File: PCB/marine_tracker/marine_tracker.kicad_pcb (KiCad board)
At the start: 2 copper layers, 71.7 x 36.4 mm, 38 parts, among them J1 Screw_Terminal_01x02, J2 Conn_ARM_JTAG_SWD_10, J4 BM04B-GHS-TBT, J5 molex_533981071, SW1 SW_Push, U1 STM32U575RGT6, U2 SHT40, U4 MIC5504-3.3YM5, U5 SAM-M10Q, U6 25CSM04T-I/SN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

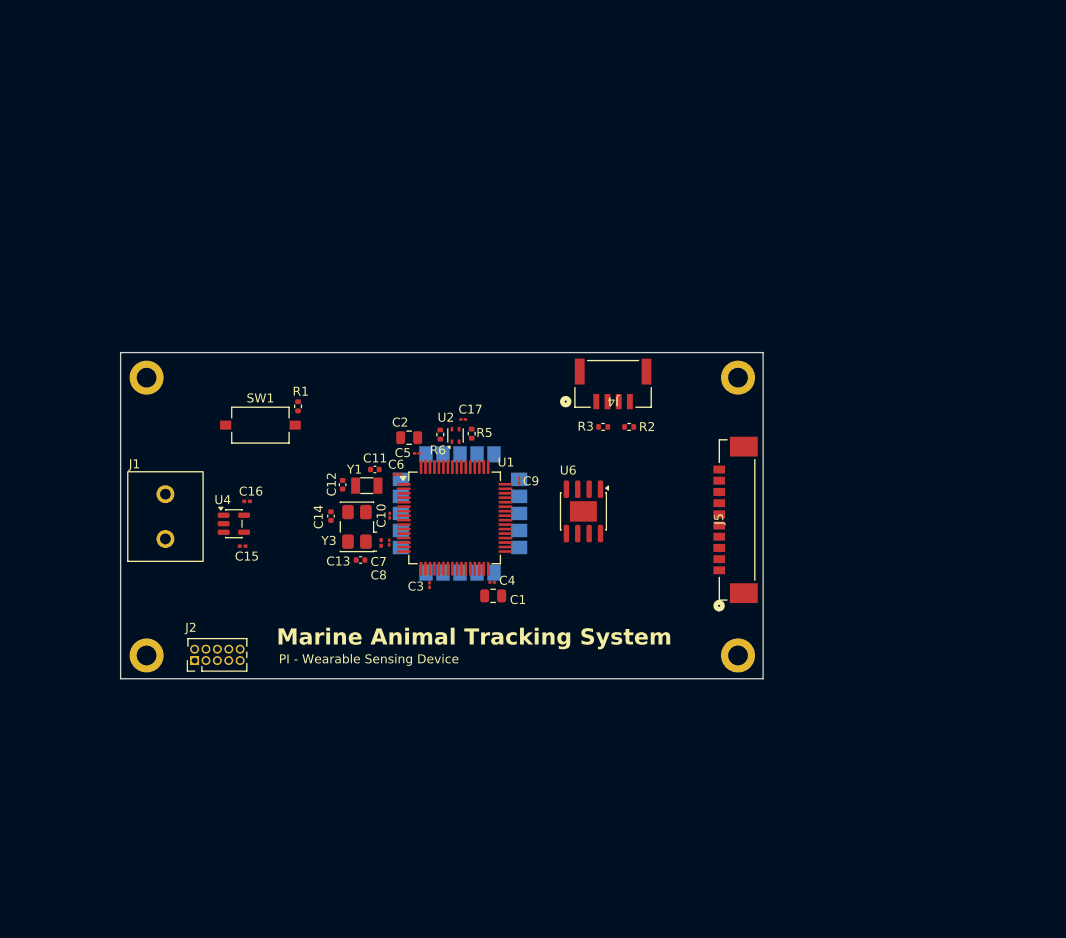
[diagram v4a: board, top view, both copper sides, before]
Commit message: routage + change GNSS module + add decoupling capacitor + change 0200/0400 package to 0600 package
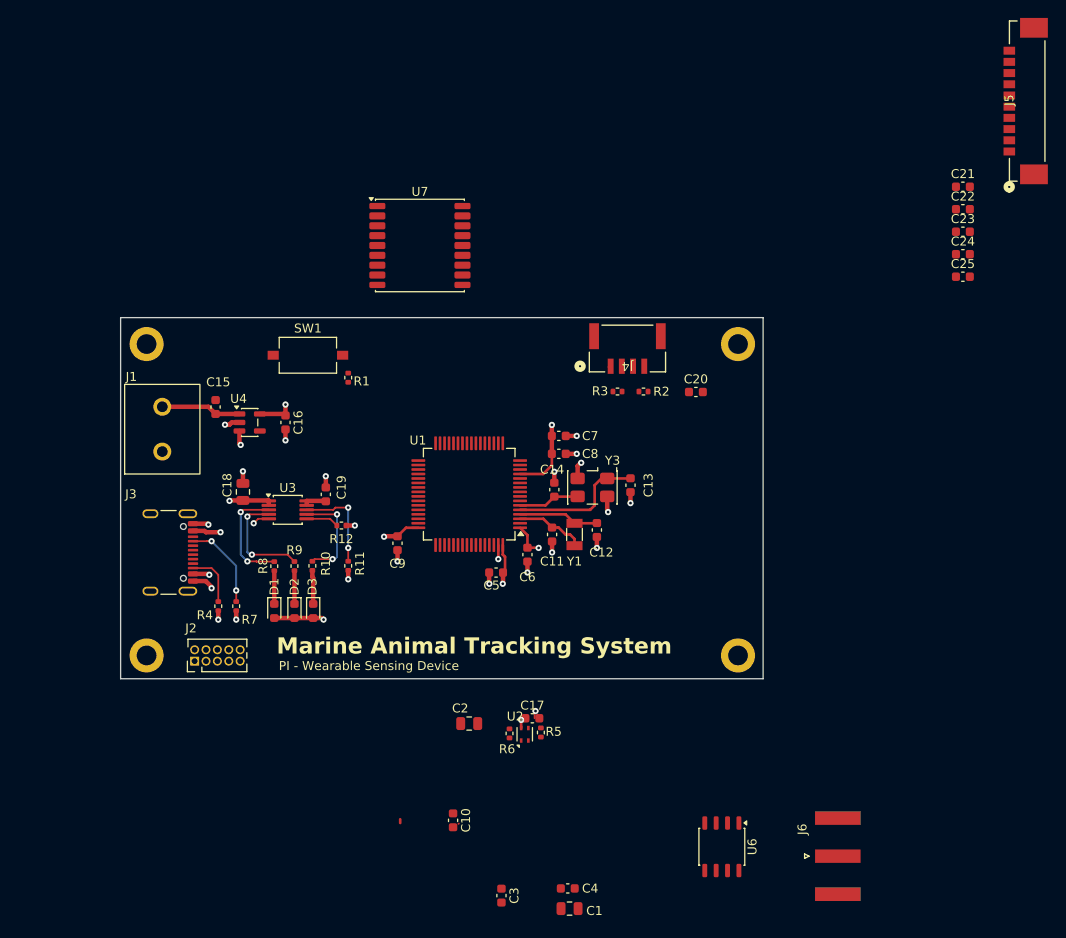
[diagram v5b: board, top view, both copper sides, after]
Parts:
- removed U5: SAM-M10Q, Beuns_PCBFootprint:XCVR_SAM-M10Q-00B
- added C18: 10u, Capacitor_SMD:C_0805_2012Metric, F.Cu at (52.2, 83.8)
- added C19: 1u, Capacitor_SMD:C_0603_1608Metric, F.Cu at (61.5, 84.0)
- added C20: 100n, Capacitor_SMD:C_0603_1608Metric, F.Cu at (102.8, 72.6)
- added C21: 100n, Capacitor_SMD:C_0603_1608Metric, F.Cu at (132.6, 49.7)
- added C22: 1n, Capacitor_SMD:C_0603_1608Metric, F.Cu at (132.6, 52.2)
- added C23: 100n, Capacitor_SMD:C_0603_1608Metric, F.Cu at (132.6, 54.7)
- added C24: 1n, Capacitor_SMD:C_0603_1608Metric, F.Cu at (132.6, 57.2)
- added C25: 100n, Capacitor_SMD:C_0603_1608Metric, F.Cu at (132.6, 59.7)
- added D1: LED, LED_SMD:LED_0603_1608Metric, F.Cu at (55.8, 97.0)
- added D2: LED, LED_SMD:LED_0603_1608Metric, F.Cu at (58.0, 97.0)
- added D3: LED, LED_SMD:LED_0603_1608Metric, F.Cu at (60.1, 97.0)
- added J3: USB_C_Receptacle_USB2.0_16P, Connector_USB:USB_C_Receptacle_GCT_USB4105-xx-A_16P_TopMnt_Horizontal, F.Cu at (43.0, 90.5)
- added J6: Conn_Coaxial, Connector_Coaxial:SMA_Amphenol_132289_EdgeMount, F.Cu at (118.6, 124.4)
- added R10: 470, Resistor_SMD:R_0402_1005Metric, F.Cu at (60.0, 92.0)
- added R11: 10k, Resistor_SMD:R_0402_1005Metric, F.Cu at (64.0, 92.0)
- added R12: 1k, Resistor_SMD:R_0402_1005Metric, F.Cu at (63.2, 87.5)
- added R4: 5k1, Resistor_SMD:R_0402_1005Metric, F.Cu at (49.5, 96.5)
- added R7: 5k1, Resistor_SMD:R_0402_1005Metric, F.Cu at (51.5, 96.5)
- added R8: 470, Resistor_SMD:R_0402_1005Metric, F.Cu at (55.8, 92.0)
- added R9: 470, Resistor_SMD:R_0402_1005Metric, F.Cu at (58.0, 92.0)
- added U3: MCP73833-xxx-UN, Package_SO:MSOP-10_3x3mm_P0.5mm, F.Cu at (57.2, 85.8)
- added U7: MAX-M10S, RF_GPS:ublox_MAX, F.Cu at (72.0, 56.2)
- C10, C17, C3, C4, C5, C8, C9: footprint Capacitor_SMD:C_01005_0402Metric -> Capacitor_SMD:C_0603_1608Metric
- C11, C12, C13, C14: footprint Capacitor_SMD:C_0402_1005Metric -> Capacitor_SMD:C_0603_1608Metric
- C15, C16, C6, C7: footprint Capacitor_SMD:C_0201_0603Metric -> Capacitor_SMD:C_0603_1608Metric
- U6: footprint Package_SO:SOIC-8-1EP_3.9x4.9mm_P1.27mm_EP2.29x3mm -> Package_SO:JEITA_SOIC-8_3.9x4.9mm_P1.27mm
- moved J5 56.9 mm to (139.8, 40.1)
- moved U6 40.5 mm to (105.7, 123.3)
- moved C1 35.9 mm to (88.7, 130.2)
- moved C3 35.6 mm to (81.1, 128.8)
- moved C4 35.2 mm to (88.5, 128.0)
- moved C10 34.7 mm to (75.7, 120.4)
- moved C17 34.2 mm to (84.5, 109.0)
- moved R6 34.2 mm to (82.0, 110.7)
- moved R5 34.2 mm to (85.5, 110.6)
- moved U2 34.2 mm to (83.7, 110.8)
- moved C2 32.6 mm to (77.5, 109.6)
- moved C13 31.3 mm to (95.5, 83.0), turned to 90 degrees
- moved C12 28.8 mm to (91.8, 88.0), turned to 90 degrees
- moved Y3 26.6 mm to (91.2, 83.2), turned to 180 degrees
- moved C14 25.1 mm to (87.0, 83.5), turned to -90 degrees
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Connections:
- net MEM_SPI1_CS renamed MEM_SPI3_CS
- U1 pad 15: MEM_SPI1_SCK -> unconnected-(U1-PA1-Pad15)
- U1 pad 44: MEM_SPI1_MISO -> USB_D-
- U1 pad 45: MEM_SPI1_MOSI -> USB_D+
- U1 pad 51: unconnected-(U1-PC10-Pad51) -> MEM_SPI1_SCK
- U1 pad 52: unconnected-(U1-PC11-Pad52) -> MEM_SPI3_MISO
- U1 pad 53: unconnected-(U1-PC12-Pad53) -> MEM_SPI3_MOSI
- U1 pad 56: unconnected-(U1-PB4-Pad56) -> GPS_LNA_EN
- U6 pad 2: MEM_SPI1_MISO -> MEM_SPI3_MISO
- U6 pad 5: MEM_SPI1_MOSI -> MEM_SPI3_MOSI
- U6 pad 6: MEM_SPI1_SCK -> MEM_SPI3_SCK
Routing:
- net GND: track 0.00 -> 34.3 mm, vias 0 -> 25
- net +3V3: track 0.00 -> 25.7 mm, vias 0 -> 5
- net VBUS: track 0.00 -> 15.4 mm, vias 0 -> 4
- net /HSE_IN: track 0.00 -> 15.1 mm
- net +BATT: track 0.00 -> 13.1 mm, vias 0 -> 1
- net /STAT1: track 0.00 -> 12.3 mm, vias 0 -> 2
- net /STAT2: track 0.00 -> 12.2 mm, vias 0 -> 2
- net /PG: track 0.00 -> 11.1 mm, vias 0 -> 2
- net /THERM: track 0.00 -> 10.7 mm, vias 0 -> 2
- net /USB_CC1: track 0.00 -> 9.95 mm, vias 0 -> 2
- net /LSE_OUT: track 0.00 -> 9.00 mm
- net /LSE_IN: track 0.00 -> 8.03 mm
- net /HSE_OUT: track 0.00 -> 6.84 mm
- net /USB_CC2: track 0.00 -> 6.12 mm
- net /LED3: track 0.00 -> 3.74 mm
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- added copper zone on In2.Cu, net +3V3
- added copper zone on In2.Cu, net +BATT
- added copper zone on In1.Cu, net GND
- added copper zone on In2.Cu, net VBUS
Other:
- board size 71.7 x 36.4 mm -> 71.7 x 40.3 mm
- copper layers 2 -> 4

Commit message: PCB routage WIP
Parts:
- moved C25 72.1 mm to (71.0, 97.2), turned to 180 degrees
- moved C1 56.7 mm to (74.0, 75.5), turned to 90 degrees
- moved C4 52.4 mm to (78.8, 76.5), turned to 90 degrees
- moved C3 52.3 mm to (71.0, 77.5), turned to 180 degrees
- moved U7 45.1 mm to (109.0, 82.0)
- moved U6 43.0 mm to (69.0, 101.0), turned to 0 degrees
- moved C20 41.9 mm to (60.9, 72.2), turned to 180 degrees
- moved J6 39.6 mm to (122.6, 85.0)
- moved C2 35.2 mm to (70.8, 75.0)
- moved R2 31.9 mm to (65.1, 72.5)
- moved J4 31.4 mm to (63.8, 67.7)
- moved R3 29.0 mm to (65.1, 74.5), turned to 180 degrees
- moved C10 26.2 mm to (85.6, 96.1), turned to 0 degrees
- moved R1 18.8 mm to (82.5, 67.5)
- moved SW1 17.1 mm to (76.5, 67.0)
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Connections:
- net USB_D+ renamed /USB_D+
- net USB_D- renamed /USB_D-
- U1 pad 51: MEM_SPI1_SCK -> MEM_SPI3_SCK
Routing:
- net SWD_NRST: track 0.00 -> 53.1 mm, vias 0 -> 4
- net /BOOT0: track 0.00 -> 33.9 mm, vias 0 -> 2
- net SWDIO: track 0.00 -> 33.8 mm, vias 0 -> 2
- net SWCLK: track 0.00 -> 32.6 mm, vias 0 -> 4
- net /USB_D-: track 0.00 -> 27.5 mm
- net /USB_D+: track 0.00 -> 27.5 mm
- net +3V3: track 25.7 -> 51.8 mm, vias 5 -> 15
- net GND: track 34.3 -> 54.5 mm, vias 25 -> 38
- net MEM_SPI3_MISO: track 0.00 -> 19.4 mm, vias 0 -> 4
- net PRES_I2C2_SDA: track 0.00 -> 19.3 mm, vias 0 -> 2
- net PRES_I2C2_SCL: track 0.00 -> 17.9 mm, vias 0 -> 2
- net SHT_SCL: track 0.00 -> 16.9 mm, vias 0 -> 2
- net SHT_SDA: track 0.00 -> 15.7 mm, vias 0 -> 4
- net MEM_SPI3_CS: track 0.00 -> 14.5 mm, vias 0 -> 2
- net MEM_SPI3_MOSI: track 0.00 -> 14.5 mm, vias 0 -> 2
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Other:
- board size 71.7 x 40.3 mm -> 87.4 x 40.3 mm

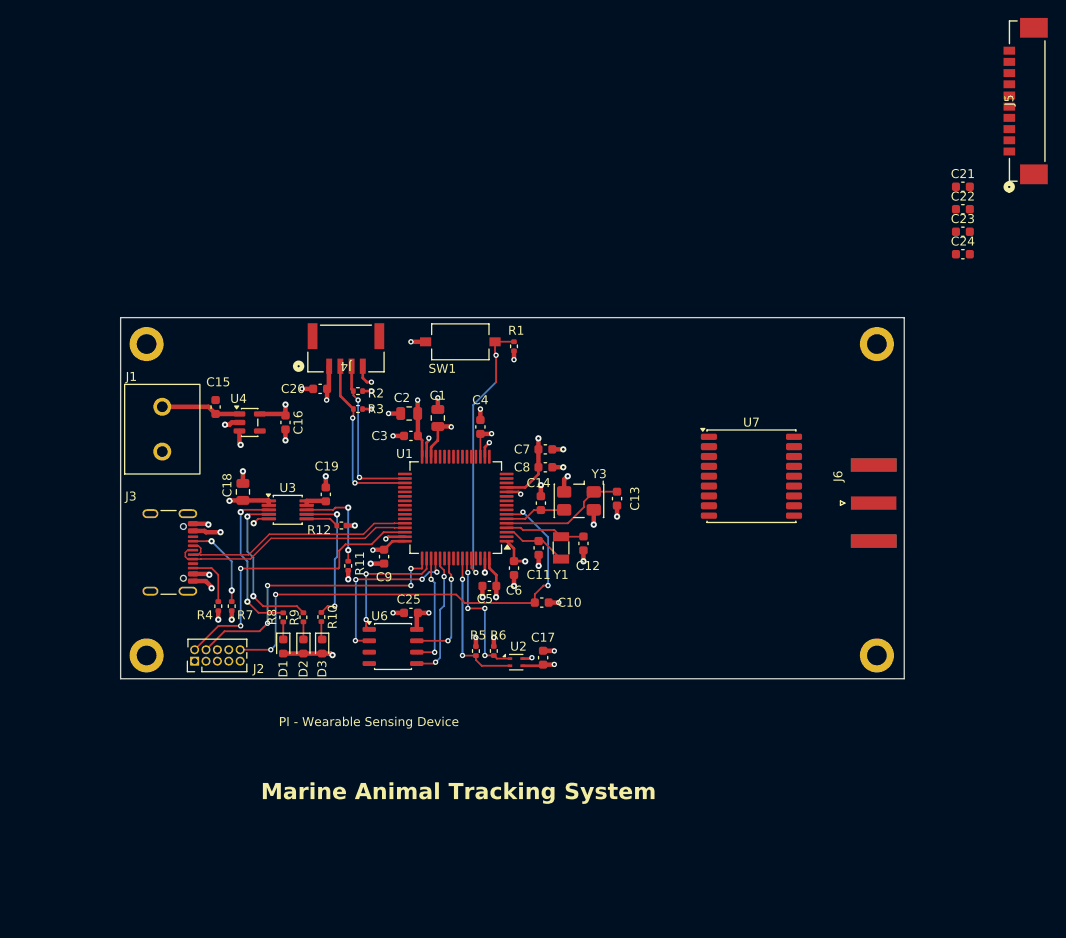
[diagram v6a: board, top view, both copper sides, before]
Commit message: add new connector for Satellite module + new LDO regulator with an maximum current higher
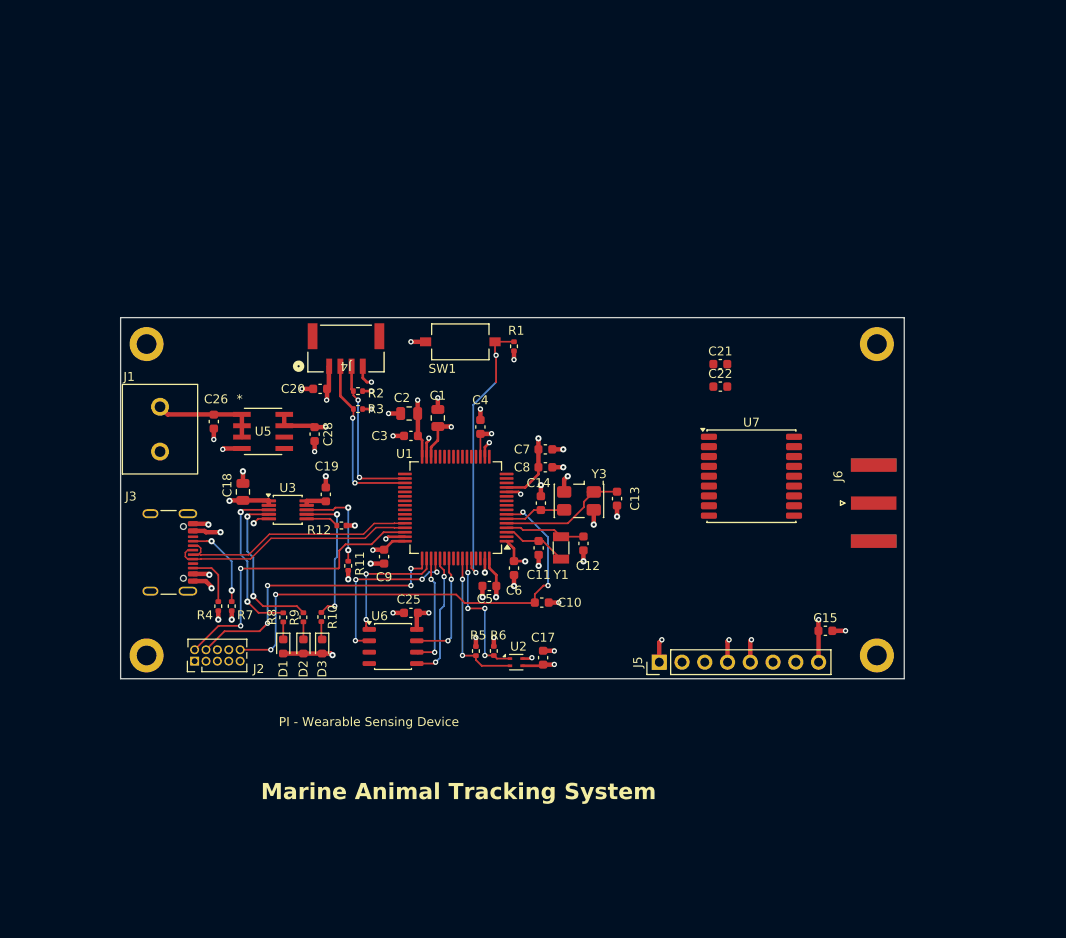
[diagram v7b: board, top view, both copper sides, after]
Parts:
- removed C16: 1u, Capacitor_SMD:C_0603_1608Metric
- removed C23: 100n, Capacitor_SMD:C_0603_1608Metric
- removed C24: 1n, Capacitor_SMD:C_0603_1608Metric
- removed U4: MIC5504-3.3YM5, Package_TO_SOT_SMD:SOT-23-5
- added C26: 4u7, Capacitor_SMD:C_0603_1608Metric, F.Cu at (49.0, 75.9)
- added C28: 1u, Capacitor_SMD:C_0603_1608Metric, F.Cu at (60.2, 77.3)
- added U5: MCP1726-3302E/SN, Beuns_PCBFootprint:SOIC8-N_MC_MCH, F.Cu at (54.5, 77.0)
- C15: value 1u -> 100n
- J5: value molex_533981071 -> Conn_01x08_Pin; footprint Beuns_PCBFootprint:CONN10_533981071_MOL -> Connector_PinHeader_2.54mm:PinHeader_1x08_P2.54mm_Vertical
- moved J5 74.9 mm to (98.7, 102.8), turned to 90 degrees
- moved C15 72.5 mm to (117.2, 99.2), turned to 0 degrees
- moved C22 33.5 mm to (105.5, 72.0)
- moved C21 33.5 mm to (105.5, 69.5)
- moved J1 0.25 mm to (43.0, 79.2)
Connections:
- C15 pad 1: +BATT -> +3V3
- J5 pad 1: SAT_RXD -> +3V3
- J5 pad 2: SAT_CTS -> SAT_RXD
- J5 pad 3: SAT_RTS -> SAT_TXD
- J5 pad 4: SAT_NetAv -> GND
- J5 pad 5: SAT_RI -> GND
- J5 pad 6: SAT_TXD -> SAT_VPA_EN
- J5 pad 7: SAT_OnOff -> SAT_VPA_SEL
- J5 pad 8: +BATT -> +3V3
- U1 pad 20: SAT_CTS -> SAT_VPA_EN
- U1 pad 21: SAT_RTS -> SAT_VPA_SEL
- U1 pad 22: SAT_NetAv -> unconnected-(U1-PA6-Pad22)
- U1 pad 23: SAT_RI -> unconnected-(U1-PA7-Pad23)
- U1 pad 41: SAT_OnOff -> unconnected-(U1-PA8-Pad41)
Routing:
- net +3V3: track 51.8 -> 60.9 mm, vias 15 -> 17
- net GND: track 54.5 -> 62.5 mm, vias 38 -> 42
- net +BATT: track 13.1 -> 14.6 mm, vias 1 -> 0

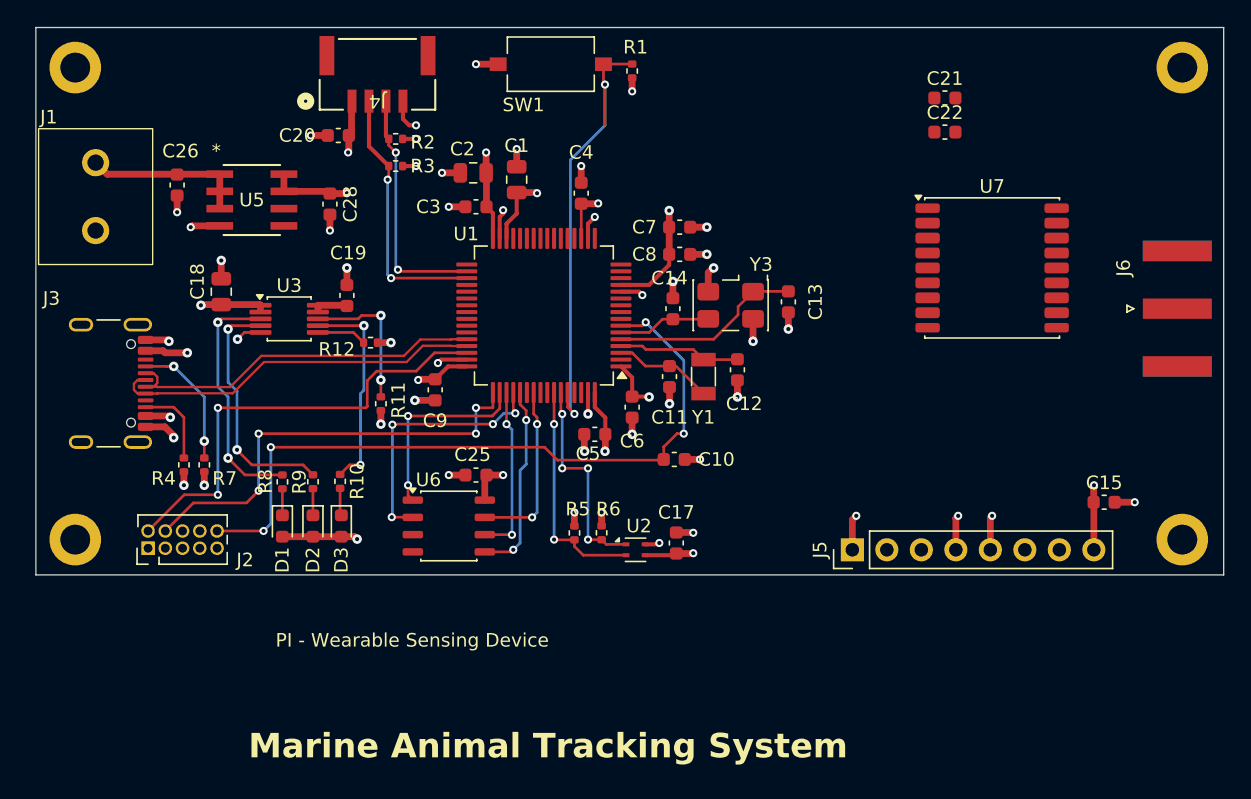
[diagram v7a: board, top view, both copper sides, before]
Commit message: change to UFL connector + add stiching via
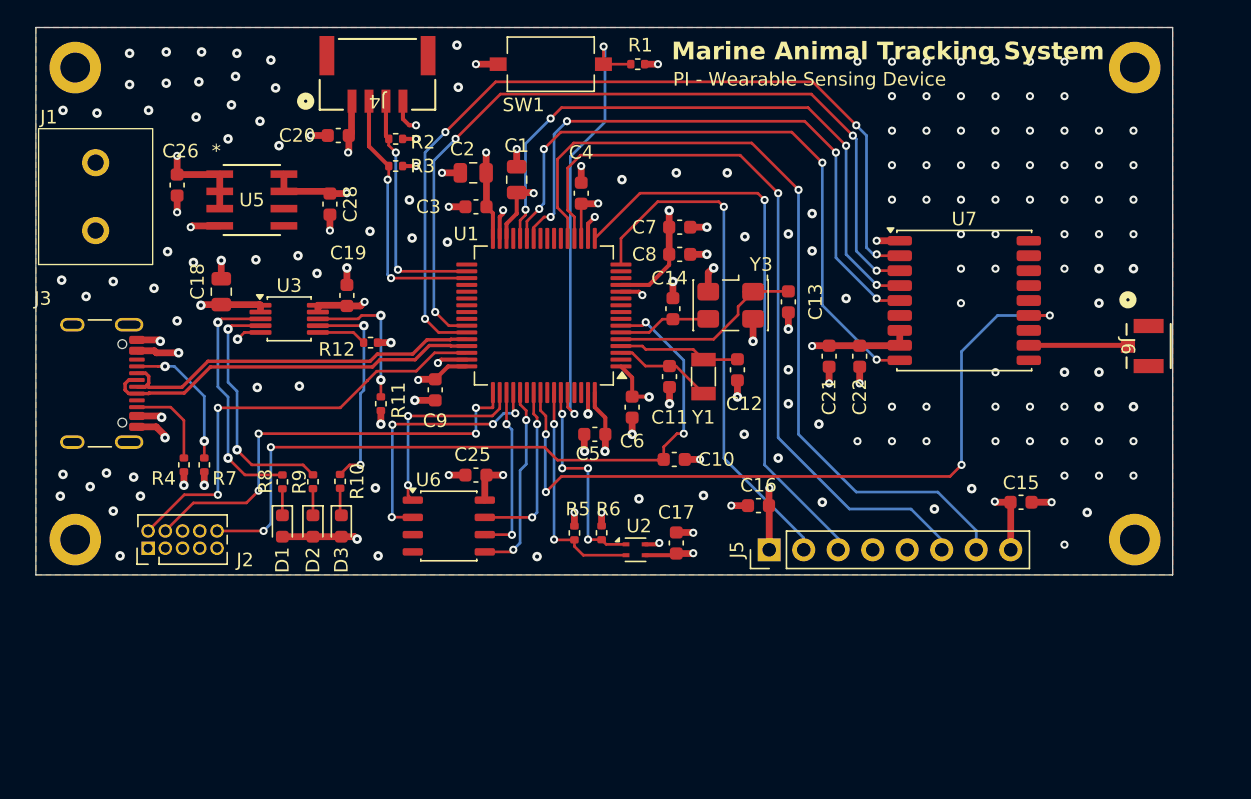
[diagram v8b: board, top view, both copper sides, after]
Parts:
- added C16: 100n, Capacitor_SMD:C_0603_1608Metric, F.Cu at (91.8, 99.5)
- J6: footprint Connector_Coaxial:SMA_Amphenol_132289_EdgeMount -> Beuns_PCBFootprint:CONN_UFL_RSP-122811-01_SAI
- moved C21 20.8 mm to (97.0, 88.5), turned to -90 degrees
- moved C22 17.7 mm to (99.2, 88.5), turned to -90 degrees
- moved C15 6.12 mm to (111.1, 99.2)
- moved J5 6.12 mm to (92.6, 102.8)
- moved J6 4.56 mm to (119.0, 87.8), turned to -90 degrees
- moved REF** 3.50 mm to (119.5, 67.2)
- moved REF** 3.50 mm to (119.5, 102.0)
- moved U7 3.16 mm to (107.0, 84.4)
- moved R1 0.65 mm to (82.9, 67.0), turned to 0 degrees
- moved J3 0.64 mm to (42.4, 90.5)
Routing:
- net GPS_TXD: track 0.00 -> 63.0 mm, vias 0 -> 4
- net SAT_VPA_SEL: track 0.00 -> 61.2 mm, vias 0 -> 1
- net GPS_RXD: track 0.00 -> 60.5 mm, vias 0 -> 4
- net GPS_LNA_EN: track 0.00 -> 56.5 mm, vias 0 -> 4
- net SAT_VPA_EN: track 0.00 -> 56.3 mm, vias 0 -> 1
- net GPS_N_RST: track 0.00 -> 46.9 mm, vias 0 -> 4
- net GPS_PULSE: track 0.00 -> 45.9 mm, vias 0 -> 4
- net GPS_EXTINT: track 0.00 -> 44.4 mm, vias 0 -> 4
- net SAT_TXD: track 0.00 -> 42.1 mm, vias 0 -> 1
- net SAT_RXD: track 0.00 -> 38.5 mm, vias 0 -> 1
- net +3V3: track 60.9 -> 70.4 mm, vias 17 -> 18
- net /RF_ANT: track 0.00 -> 7.39 mm
- net +BATT: track 14.6 -> 11.0 mm, vias 0 -> 2
- net SWDIO: track 33.8 -> 32.7 mm
- net /USB_D-: track 27.5 -> 28.2 mm
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- added copper zone on F.Cu, net GND
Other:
- board size 87.4 x 40.3 mm -> 83.7 x 40.3 mm
